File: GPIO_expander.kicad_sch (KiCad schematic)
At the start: 2 parts, among them U3 TCA9535PWR

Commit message: done ( v 1.0 - check required )
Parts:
- C3: footprint (none) -> PCM_JLCPCB:C_0603
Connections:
- net GPIO_6: now reaches U3.10 (P06)
- net GPIO_7: now reaches U3.11 (P07)
- net GPIO_8: now reaches U3.13 (P10)
- net GPIO_4: now reaches U3.8 (P04)
- net GPIO_5: now reaches U3.9 (P05)
- net +3.3V renamed +3V3
- no-connect marks 1 -> 8
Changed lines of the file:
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@@
+	)
+	(no_connect
+		(at 160.02 110.49)
+	)
+	(no_connect
+		(at 160.02 105.41)
 	)
 	(no_connect
 		(at 124.46 82.55)
+	)
+	(no_connect
+		(at 160.02 102.87)
+	)
+	(no_connect
+		(at 160.02 118.11)
+	)
+	(no_connect
+		(at 160.02 115.57)
+	)
+	(no_connect
+		(at 160.02 113.03)
+	)
+	(no_connect
+		(at 160.02 107.95)
 	)
 	(bus_entry
@@
 	(wire
 		(pts
+			(xy 160.02 92.71) (xy 165.1 92.71)
+		)
+		(stroke
+			(width 0)
+			(type default)
+		)
+	)
+	(wire
+		(pts
 			(xy 160.02 85.09) (xy 165.1 85.09)
 		)
@@
 	(wire
 		(pts
+			(xy 160.02 87.63) (xy 165.1 87.63)
+		)
+		(stroke
+			(width 0)
+			(type default)
+		)
+	)
+	(wire
+		(pts
+			(xy 160.02 95.25) (xy 165.1 95.25)
+		)
+		(stroke
+			(width 0)
+			(type default)
+		)
+	)
+	(wire
+		(pts
 			(xy 160.02 77.47) (xy 165.1 77.47)
 		)
@@
 	(wire
 		(pts
+			(xy 160.02 100.33) (xy 165.1 100.33)
+		)
+		(stroke
+			(width 0)
+			(type default)
+		)
+	)
+	(wire
+		(pts
 			(xy 124.46 113.03) (xy 124.46 115.57)
+		)
+		(stroke
+			(width 0)
+			(type default)
+		)
+	)
+	(wire
+		(pts
+			(xy 160.02 90.17) (xy 165.1 90.17)
 		)
 		(stroke
@@
 		)
 	)
+	(hierarchical_label "GPIO_8"
+		(shape input)
+		(at 165.1 100.33 0)
+		(effects
+			(font
+				(size 1.27 1.27)
+			)
+			(justify left)
+		)
+	)
 	(hierarchical_label "GPIO_1"
 		(shape input)
@@
 		)
 	)
+	(hierarchical_label "GPIO_4"
+		(shape input)
+		(at 165.1 87.63 0)
+		(effects
+			(font
+				(size 1.27 1.27)
+			)
+			(justify left)
+		)
+	)
+	(hierarchical_label "GPIO_6"
+		(shape input)
+		(at 165.1 92.71 0)
+		(effects
+			(font
+				(size 1.27 1.27)
+			)
+			(justify left)
+		)
+	)
 	(hierarchical_label "GPIO_2"
 		(shape input)
@@
 		(shape input)
 		(at 165.1 85.09 0)
+		(effects
+			(font
+				(size 1.27 1.27)
+			)
+			(justify left)
+		)
+	)
+	(hierarchical_label "GPIO_7"
+		(shape input)
+		(at 165.1 95.25 0)
+		(effects
+			(font
+				(size 1.27 1.27)
+			)
+			(justify left)
+		)
+	)
+	(hierarchical_label "GPIO_5"
+		(shape input)
+		(at 165.1 90.17 0)
 		(effects
 			(font
@@
 	)
 	(symbol
-		(lib_id "power:+3.3V")
-		(at 93.98 96.52 0)
-		(unit 1)
-		(exclude_from_sim no)
-		(in_bom yes)
-		(on_board yes)
-		(dnp no)
-		(fields_autoplaced yes)
-		(property "Reference" "#PWR046"
-			(at 93.98 100.33 0)
-			(effects
-				(font
-					(size 1.27 1.27)
-				)
-				(hide yes)
-			)
-		)
-		(property "Value" "+3.3V"
-			(at 93.98 91.44 0)
-			(effects
-				(font
-					(size 1.27 1.27)
-				)
-			)
-		)
-		(property "Footprint" ""
-			(at 93.98 96.52 0)
-			(effects
-				(font
-					(size 1.27 1.27)
-				)
-				(hide yes)
-			)
-		)
-		(property "Datasheet" ""
-			(at 93.98 96.52 0)
-			(effects
-				(font
-					(size 1.27 1.27)
-				)
-				(hide yes)
-			)
-		)
-		(property "Description" "Power symbol creates a global label with name \"+3.3V\""
-			(at 93.98 96.52 0)
-			(effects
-				(font
-					(size 1.27 1.27)
-				)
-				(hide yes)
-			)
-		)
-		(pin "1"
-		)
-		(instances
-			(project ""
-				(path "/6596548a-44e0-46d8-8624-fd71cf4a3e17/759d6f3d-0961-4f50-af85-ab5d1408915a"
-					(reference "#PWR046")
-					(unit 1)
-				)
-			)
-		)
-	)
-	(symbol
 		(lib_id "power:GND")
 		(at 93.98 104.14 0)
@@
 			)
 		)
-		(property "Footprint" ""
+		(property "Footprint" "PCM_JLCPCB:C_0603"
 			(at 94.9452 104.14 0)
 			(effects
@@
 	)
 	(symbol
-		(lib_id "power:+3.3V")
-		(at 142.24 69.85 0)
-		(unit 1)
-		(exclude_from_sim no)
-		(in_bom yes)
-		(on_board yes)
-		(dnp no)
-		(fields_autoplaced yes)
-		(property "Reference" "#PWR039"
-			(at 142.24 73.66 0)
-			(effects
-				(font
-					(size 1.27 1.27)
-				)
-				(hide yes)
-			)
-		)
-		(property "Value" "+3.3V"
-			(at 142.24 64.77 0)
-			(effects
-				(font
-					(size 1.27 1.27)
-				)
-			)
-		)
-		(property "Footprint" ""
-			(at 142.24 69.85 0)
-			(effects
-				(font
-					(size 1.27 1.27)
-				)
-				(hide yes)
-			)
-		)
-		(property "Datasheet" ""
-			(at 142.24 69.85 0)
-			(effects
-				(font
-					(size 1.27 1.27)
-				)
-				(hide yes)
-			)
-		)
-		(property "Description" "Power symbol creates a global label with name \"+3.3V\""
-			(at 142.24 69.85 0)
-			(effects
-				(font
-					(size 1.27 1.27)
-				)
-				(hide yes)
-			)
-		)
-		(pin "1"
-		)
-		(instances
-			(project ""
-				(path "/6596548a-44e0-46d8-8624-fd71cf4a3e17/759d6f3d-0961-4f50-af85-ab5d1408915a"
-					(reference "#PWR039")
-					(unit 1)
-				)
-			)
-		)
-	)
-	(symbol
 		(lib_id "power:GND")
 		(at 124.46 119.38 0)
@@
 					(unit 1)
 				)
+			)
+		)
+	)
+	(symbol
+		(lib_id "power:+5V")
+		(at 142.24 69.85 0)
+		(unit 1)
+		(exclude_from_sim no)
+		(in_bom yes)
+		(on_board yes)
+		(dnp no)
+		(fields_autoplaced yes)
+		(property "Reference" "#PWR039"
+			(at 142.24 73.66 0)
+			(effects
+				(font
+					(size 1.27 1.27)
+				)
+				(hide yes)
+			)
+		)
+		(property "Value" "+3V3"
+			(at 142.24 64.77 0)
+			(effects
+				(font
+					(size 1.27 1.27)
+				)
+			)
+		)
+		(property "Footprint" ""
+			(at 142.24 69.85 0)
+			(effects
+				(font
+					(size 1.27 1.27)
+				)
+				(hide yes)
+			)
+		)
+		(property "Datasheet" ""
+			(at 142.24 69.85 0)
+			(effects
+				(font
+					(size 1.27 1.27)
+				)
+				(hide yes)
+			)
+		)
+		(property "Description" "Power symbol creates a global label with name \"+5V\""
+			(at 142.24 69.85 0)
+			(effects
+				(font
+					(size 1.27 1.27)
+				)
+				(hide yes)
+			)
+		)
+		(pin "1"
+		)
+		(instances
+			(project "MMS3_hat_templates"
+				(path "/6596548a-44e0-46d8-8624-fd71cf4a3e17/759d6f3d-0961-4f50-af85-ab5d1408915a"
+					(reference "#PWR039")
+					(unit 1)
+				)
+			)
+		)
+	)
+	(symbol
+		(lib_id "power:+5V")
+		(at 93.98 96.52 0)
+		(unit 1)
+		(exclude_from_sim no)
+		(in_bom yes)
+		(on_board yes)
+		(dnp no)
+		(fields_autoplaced yes)
+		(property "Reference" "#PWR046"
+			(at 93.98 100.33 0)
+			(effects
+				(font
+					(size 1.27 1.27)
+				)
+				(hide yes)
+			)
+		)
+		(property "Value" "+3V3"
+			(at 93.98 91.44 0)
+			(effects
+				(font
+					(size 1.27 1.27)
+				)
+			)
+		)
+		(property "Footprint" ""
+			(at 93.98 96.52 0)
+			(effects
+				(font
+					(size 1.27 1.27)
+				)
+				(hide yes)
+			)
+		)
+		(property "Datasheet" ""
+			(at 93.98 96.52 0)
+			(effects
+				(font
+					(size 1.27 1.27)
+				)
+				(hide yes)
+			)
+		)
+		(property "Description" "Power symbol creates a global label with name \"+5V\""
+			(at 93.98 96.52 0)
+			(effects
+				(font
+					(size 1.27 1.27)
+				)
+				(hide yes)
+			)
+		)
+		(pin "1"
+		)
+		(instances
+			(project "MMS3_hat_templates"
+				(path "/6596548a-44e0-46d8-8624-fd71cf4a3e17/759d6f3d-0961-4f50-af85-ab5d1408915a"
+					(reference "#PWR046")
+					(unit 1)
+				)

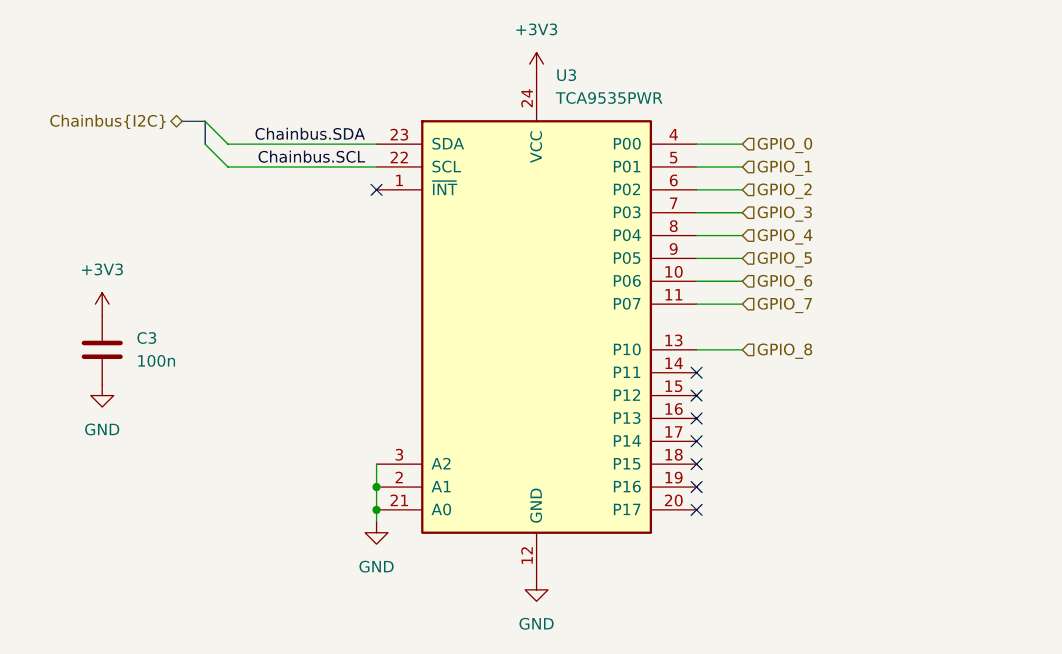
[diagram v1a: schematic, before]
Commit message: fixed selected led polarity
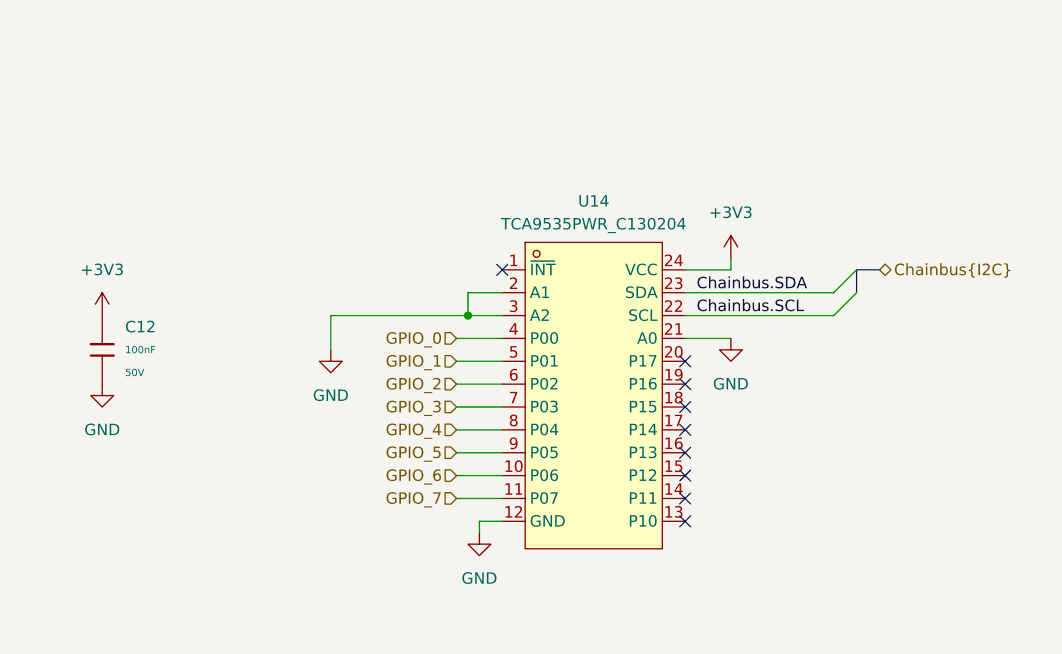
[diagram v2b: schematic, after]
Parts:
- removed C3: 100n, PCM_JLCPCB:C_0603, symbol Device:C
- removed U3: TCA9535PWR, Package_SO:TSSOP-24_4.4x7.8mm_P0.65mm, symbol Interface_Expansion:TCA9535PWR
- added C12: 100nF, PCM_JLCPCB:C_0603, symbol PCM_JLCPCB-Capacitors:0603,100nF
- added U14: TCA9535PWR_C130204, TCA9535PWR:TSSOP-24_L7.8-W4.4-P0.65-LS6.4-BL, symbol TCA9535PWR1:TCA9535PWR_C130204
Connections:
- net +3V3: now also C12.1, U14.24 (VCC)
- net Chainbus.SCL: now also U14.22 (SCL)
- net Chainbus.SDA: now also U14.23 (SDA)
- net GND: now also C12.2, U14.12 (GND), U14.2 (A1), U14.21 (A0), U14.3 (A2)
- net GPIO_0: now also U14.4 (P00)
- net GPIO_1: now also U14.5 (P01)
- net GPIO_2: now also U14.6 (P02)
- net GPIO_3: now also U14.7 (P03)
- net GPIO_4: now also U14.8 (P04)
- net GPIO_5: now also U14.9 (P05)
- net GPIO_6: now also U14.10 (P06)
- net GPIO_7: now also U14.11 (P07)
- no-connect marks 8 -> 9
